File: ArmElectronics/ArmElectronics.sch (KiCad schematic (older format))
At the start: 91 parts, among them J1 Raspberry_Pi_2_3, J10 AH1815 Breakout, J11 AH1815 Breakout, J12 AH1815 Breakout, J13 AH1815 Breakout, J14 AH1815 Breakout, J15 AH1815 Breakout, J16 AH1815 Breakout, J17 AH1815 Breakout, J18 AH1815 Breakout, J19 AH1815 Breakout, J2 Conn_01x14, J20 AH1815 Breakout, J21 1792245, J22 PA-09, J23 PA-09, J24 PA-09, J3 Encoder Breakout, J4 RasPi Power Out, J5 12V In, J6 Batt In, J7 Batt Out, J8 BNO055 QWIIC Conn, J9 AH1815 Breakout, SW1 E-Stop, U1 Teensy4.1, U12 74LVC1G97, U13 74LVC1G97, U14 74LVC1G97, U15 74LVC1G97, U16 74LVC1G97, U17 74LVC1G97, U2 Pololu_2857, U3 MAX11601, U4 Pololu_2851, U5 Pololu_3730, U6 TB9051FTG, U7 TB9051FTG, U8 TB9051FTG

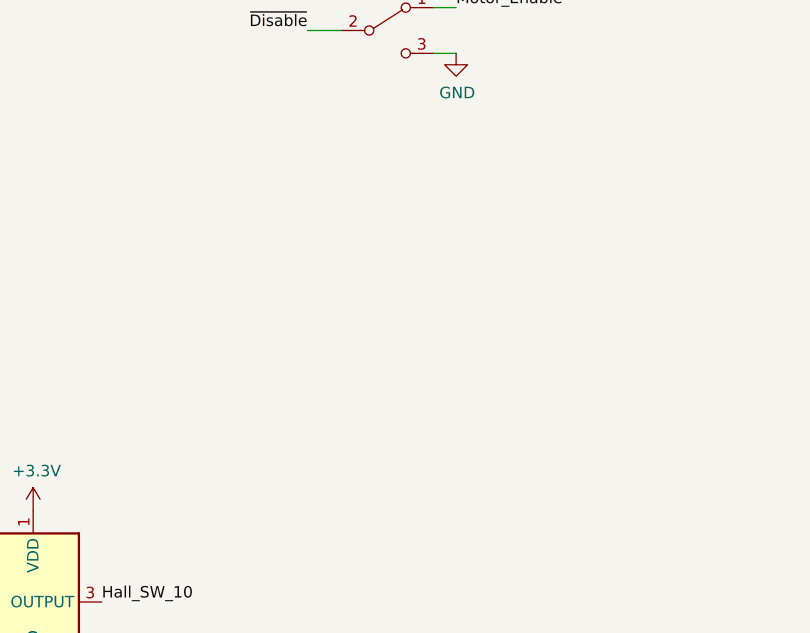
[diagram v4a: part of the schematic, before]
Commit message: Added brake solenoid for axis 0
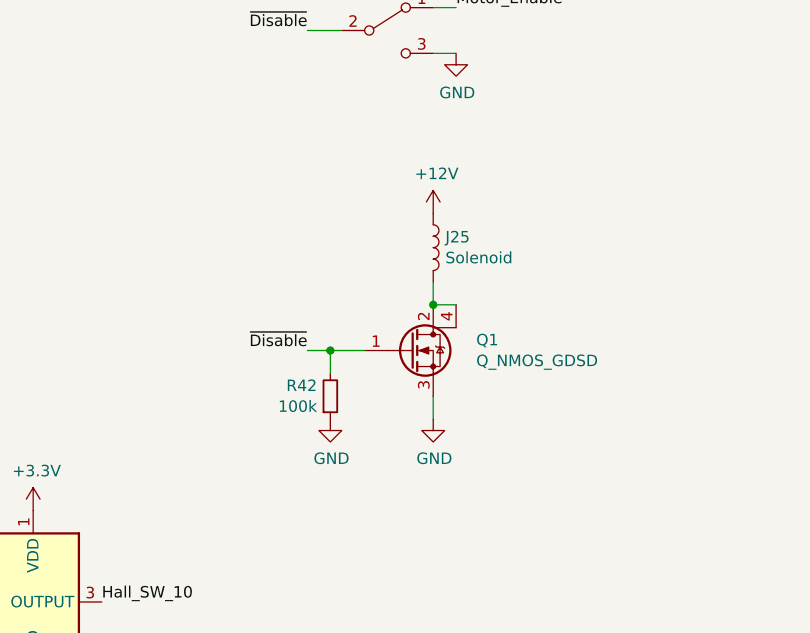
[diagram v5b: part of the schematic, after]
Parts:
- added J25: Solenoid, Connector_JST:JST_XH_B2B-XH-A_1x02_P2.50mm_Vertical, symbol Device:L
- added Q1: Q_NMOS_GDSD, Package_TO_SOT_SMD:SOT-223, symbol Device:Q_NMOS_GDSD
- added R42: 100k, Resistor_SMD:R_0603_1608Metric_Pad1.05x0.95mm_HandSolder, symbol Device:R_Small
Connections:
- net +12V: now also J25.1
- net GND: now also Q1.3 (S), R42.1
- net ~Disable: now also Q1.1 (G), R42.2
- new net: J25.2, Q1.2 (D), Q1.4 (D)
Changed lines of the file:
@@
 Wire Wire Line
 	3100 2250 2900 2250
+$Comp
+L Device:L J25
+U 1 1 5FBC5F32
+P 12950 10450
+F 0 "J25" H 13003 10496 50  0000 L CNN
+F 1 "Solenoid" H 13003 10405 50  0000 L CNN
+F 2 "Connector_JST:JST_XH_B2B-XH-A_1x02_P2.50mm_Vertical" H 12950 10450 50  0001 C CNN
+F 3 "~" H 12950 10450 50  0001 C CNN
+	1    12950 10450
+	1    0    0    -1
+$EndComp
+$Comp
+L Device:Q_NMOS_GDSD Q1
+U 1 1 5FBC8FF5
+P 12850 10900
+F 0 "Q1" H 13138 10946 50  0000 L CNN
+F 1 "Q_NMOS_GDSD" H 13138 10855 50  0000 L CNN
+F 2 "Package_TO_SOT_SMD:SOT-223" H 13050 11000 50  0001 C CNN
+F 3 "~" H 12850 10900 50  0001 C CNN
+F 4 "NCV8440ASTT1GOSCT-ND" H 12850 10900 50  0001 C CNN "Digikey Part Num"
+	1    12850 10900
+	1    0    0    -1
+$EndComp
+$Comp
+L Device:R_Small R42
+U 1 1 5FBCC898
+P 12500 11100
+F 0 "R42" H 12442 11054 50  0000 R CNN
+F 1 "100k" H 12442 11145 50  0000 R CNN
+F 2 "Resistor_SMD:R_0603_1608Metric_Pad1.05x0.95mm_HandSolder" H 12500 11100 50  0001 C CNN
+F 3 "~" H 12500 11100 50  0001 C CNN
+F 4 "P100KGCT-ND" H 12500 11100 50  0001 C CNN "Digikey Part Num"
+	1    12500 11100
+	1    0    0    1
+$EndComp
+Wire Wire Line
+	12400 10900 12500 10900
+Wire Wire Line
+	12500 11000 12500 10900
+Connection ~ 12500 10900
+Wire Wire Line
+	12500 10900 12650 10900
+$Comp
+L power:GND #PWR0126
+U 1 1 5FC1211A
+P 12500 11200
+F 0 "#PWR0126" H 12500 10950 50  0001 C CNN
+F 1 "GND" H 12505 11027 50  0000 C CNN
+F 2 "" H 12500 11200 50  0001 C CNN
+F 3 "" H 12500 11200 50  0001 C CNN
+	1    12500 11200
+	1    0    0    -1
+$EndComp
+Wire Wire Line
+	13050 10700 12950 10700
+Wire Wire Line
+	12950 10700 12950 10600
+Connection ~ 12950 10700
+$Comp
+L power:GND #PWR0127
+U 1 1 5FC36123
+P 12950 11200
+F 0 "#PWR0127" H 12950 10950 50  0001 C CNN
+F 1 "GND" H 12955 11027 50  0000 C CNN
+F 2 "" H 12950 11200 50  0001 C CNN
+F 3 "" H 12950 11200 50  0001 C CNN
+	1    12950 11200
+	1    0    0    -1
+$EndComp
+Wire Wire Line
+	12950 11200 12950 11100
+$Comp
+L power:+12V #PWR060
+U 1 1 5FC71FCB
+P 12950 10300
+F 0 "#PWR060" H 12950 10150 50  0001 C CNN
+F 1 "+12V" H 12965 10473 50  0000 C CNN
+F 2 "" H 12950 10300 50  0001 C CNN
+F 3 "" H 12950 10300 50  0001 C CNN
+	1    12950 10300
+	1    0    0    -1
+$EndComp
+Text Label 12400 10900 2    50   ~ 0
+~Disable
 $EndSCHEMATC

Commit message: Added some 3d models
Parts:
- J10, J11, J12, J13, J14, J15, J16, J17, J18, J19, J20, J9: footprint Connector_JST:JST_PH_S3B-PH-K_1x03_P2.00mm_Horizontal -> Connector_JST:JST_PH_B3B-PH-K_1x03_P2.00mm_Vertical
- J3: footprint Connector_JST:JST_PH_S6B-PH-K_1x06_P2.00mm_Horizontal -> Connector_JST:JST_PH_B6B-PH-K_1x06_P2.00mm_Vertical
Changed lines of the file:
@@
 F 0 "J9" H 7270 12046 50  0000 R CNN
 F 1 "AH1815 Breakout" H 7270 11955 50  0000 R CNN
-F 2 "Connector_JST:JST_PH_S3B-PH-K_1x03_P2.00mm_Horizontal" H 7500 12000 50  0001 C CNN
+F 2 "Connector_JST:JST_PH_B3B-PH-K_1x03_P2.00mm_Vertical" H 7500 12000 50  0001 C CNN
 F 3 "https://www.diodes.com/assets/Datasheets/AH1806.pdf" H 7500 12000 50  0001 C CNN
 	1    7500 12000
@@
 F 0 "J3" H 9480 10592 50  0000 L CNN
 F 1 "Encoder Breakout" H 9480 10501 50  0000 L CNN
-F 2 "Connector_JST:JST_PH_S6B-PH-K_1x06_P2.00mm_Horizontal" H 9400 10600 50  0001 C CNN
+F 2 "Connector_JST:JST_PH_B6B-PH-K_1x06_P2.00mm_Vertical" H 9400 10600 50  0001 C CNN
 F 3 "~" H 9400 10600 50  0001 C CNN
 	1    9400 10600
@@
 F 0 "J10" H 7270 13346 50  0000 R CNN
 F 1 "AH1815 Breakout" H 7270 13255 50  0000 R CNN
-F 2 "Connector_JST:JST_PH_S3B-PH-K_1x03_P2.00mm_Horizontal" H 7500 13300 50  0001 C CNN
+F 2 "Connector_JST:JST_PH_B3B-PH-K_1x03_P2.00mm_Vertical" H 7500 13300 50  0001 C CNN
 F 3 "https://www.diodes.com/assets/Datasheets/AH1806.pdf" H 7500 13300 50  0001 C CNN
 	1    7500 13300
@@
 F 0 "J11" H 7270 14646 50  0000 R CNN
 F 1 "AH1815 Breakout" H 7270 14555 50  0000 R CNN
-F 2 "Connector_JST:JST_PH_S3B-PH-K_1x03_P2.00mm_Horizontal" H 7500 14600 50  0001 C CNN
+F 2 "Connector_JST:JST_PH_B3B-PH-K_1x03_P2.00mm_Vertical" H 7500 14600 50  0001 C CNN
 F 3 "https://www.diodes.com/assets/Datasheets/AH1806.pdf" H 7500 14600 50  0001 C CNN
 	1    7500 14600
@@
 F 0 "J12" H 8520 12046 50  0000 R CNN
 F 1 "AH1815 Breakout" H 8520 11955 50  0000 R CNN
-F 2 "Connector_JST:JST_PH_S3B-PH-K_1x03_P2.00mm_Horizontal" H 8750 12000 50  0001 C CNN
+F 2 "Connector_JST:JST_PH_B3B-PH-K_1x03_P2.00mm_Vertical" H 8750 12000 50  0001 C CNN
 F 3 "https://www.diodes.com/assets/Datasheets/AH1806.pdf" H 8750 12000 50  0001 C CNN
 	1    8750 12000
@@
 F 0 "J13" H 8520 13346 50  0000 R CNN
 F 1 "AH1815 Breakout" H 8520 13255 50  0000 R CNN
-F 2 "Connector_JST:JST_PH_S3B-PH-K_1x03_P2.00mm_Horizontal" H 8750 13300 50  0001 C CNN
+F 2 "Connector_JST:JST_PH_B3B-PH-K_1x03_P2.00mm_Vertical" H 8750 13300 50  0001 C CNN
 F 3 "https://www.diodes.com/assets/Datasheets/AH1806.pdf" H 8750 13300 50  0001 C CNN
 	1    8750 13300
@@
 F 0 "J14" H 8520 14646 50  0000 R CNN
 F 1 "AH1815 Breakout" H 8520 14555 50  0000 R CNN
-F 2 "Connector_JST:JST_PH_S3B-PH-K_1x03_P2.00mm_Horizontal" H 8750 14600 50  0001 C CNN
+F 2 "Connector_JST:JST_PH_B3B-PH-K_1x03_P2.00mm_Vertical" H 8750 14600 50  0001 C CNN
 F 3 "https://www.diodes.com/assets/Datasheets/AH1806.pdf" H 8750 14600 50  0001 C CNN
 	1    8750 14600
@@
 F 0 "J15" H 9720 12046 50  0000 R CNN
 F 1 "AH1815 Breakout" H 9720 11955 50  0000 R CNN
-F 2 "Connector_JST:JST_PH_S3B-PH-K_1x03_P2.00mm_Horizontal" H 9950 12000 50  0001 C CNN
+F 2 "Connector_JST:JST_PH_B3B-PH-K_1x03_P2.00mm_Vertical" H 9950 12000 50  0001 C CNN
 F 3 "https://www.diodes.com/assets/Datasheets/AH1806.pdf" H 9950 12000 50  0001 C CNN
 	1    9950 12000
@@
 F 0 "J16" H 9770 13346 50  0000 R CNN
 F 1 "AH1815 Breakout" H 9770 13255 50  0000 R CNN
-F 2 "Connector_JST:JST_PH_S3B-PH-K_1x03_P2.00mm_Horizontal" H 10000 13300 50  0001 C CNN
+F 2 "Connector_JST:JST_PH_B3B-PH-K_1x03_P2.00mm_Vertical" H 10000 13300 50  0001 C CNN
 F 3 "https://www.diodes.com/assets/Datasheets/AH1806.pdf" H 10000 13300 50  0001 C CNN
 	1    10000 13300
@@
 F 0 "J17" H 9770 14646 50  0000 R CNN
 F 1 "AH1815 Breakout" H 9770 14555 50  0000 R CNN
-F 2 "Connector_JST:JST_PH_S3B-PH-K_1x03_P2.00mm_Horizontal" H 10000 14600 50  0001 C CNN
+F 2 "Connector_JST:JST_PH_B3B-PH-K_1x03_P2.00mm_Vertical" H 10000 14600 50  0001 C CNN
 F 3 "https://www.diodes.com/assets/Datasheets/AH1806.pdf" H 10000 14600 50  0001 C CNN
 	1    10000 14600
@@
 F 0 "J18" H 10970 12046 50  0000 R CNN
 F 1 "AH1815 Breakout" H 10970 11955 50  0000 R CNN
-F 2 "Connector_JST:JST_PH_S3B-PH-K_1x03_P2.00mm_Horizontal" H 11200 12000 50  0001 C CNN
+F 2 "Connector_JST:JST_PH_B3B-PH-K_1x03_P2.00mm_Vertical" H 11200 12000 50  0001 C CNN
 F 3 "https://www.diodes.com/assets/Datasheets/AH1806.pdf" H 11200 12000 50  0001 C CNN
 	1    11200 12000
@@
 F 0 "J19" H 11020 13346 50  0000 R CNN
 F 1 "AH1815 Breakout" H 11020 13255 50  0000 R CNN
-F 2 "Connector_JST:JST_PH_S3B-PH-K_1x03_P2.00mm_Horizontal" H 11250 13300 50  0001 C CNN
+F 2 "Connector_JST:JST_PH_B3B-PH-K_1x03_P2.00mm_Vertical" H 11250 13300 50  0001 C CNN
 F 3 "https://www.diodes.com/assets/Datasheets/AH1806.pdf" H 11250 13300 50  0001 C CNN
 	1    11250 13300
@@
 F 0 "J20" H 11020 14646 50  0000 R CNN
 F 1 "AH1815 Breakout" H 11020 14555 50  0000 R CNN
-F 2 "Connector_JST:JST_PH_S3B-PH-K_1x03_P2.00mm_Horizontal" H 11250 14600 50  0001 C CNN
+F 2 "Connector_JST:JST_PH_B3B-PH-K_1x03_P2.00mm_Vertical" H 11250 14600 50  0001 C CNN
 F 3 "https://www.diodes.com/assets/Datasheets/AH1806.pdf" H 11250 14600 50  0001 C CNN
 	1    11250 14600

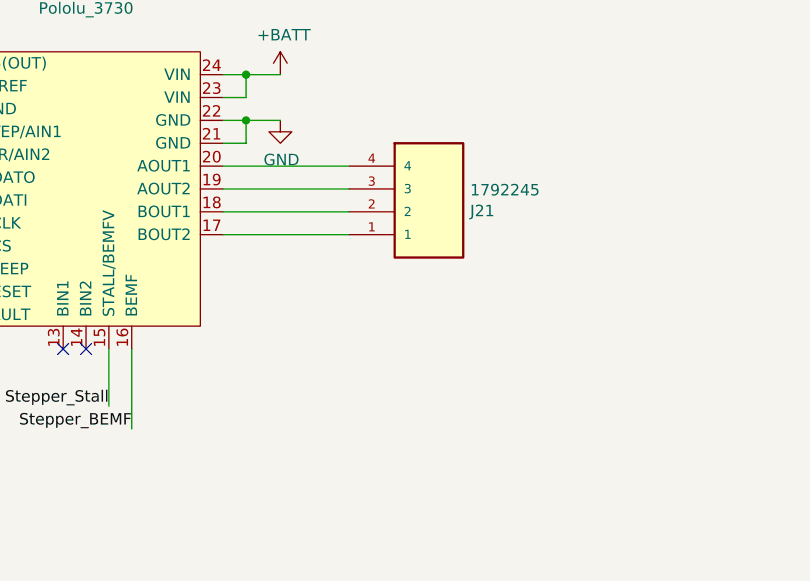
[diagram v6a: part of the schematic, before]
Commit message: added an alternate stepper connector
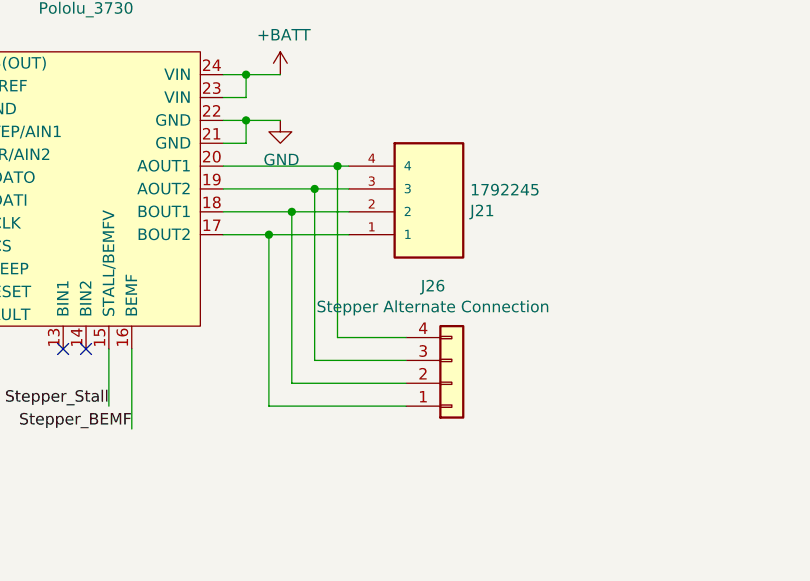
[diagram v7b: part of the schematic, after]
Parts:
- added J26: Stepper Alternate Connection, Connector_JST:JST_XH_S4B-XH-A_1x04_P2.50mm_Horizontal, symbol Connector_Generic:Conn_01x04
- J10, J11, J12, J13, J14, J15, J16, J17, J18, J19, J20, J9, SW1: Digikey Part Num (none) -> 455-1705-ND
- J25: Digikey Part Num (none) -> 455-2247-ND
- J3: Digikey Part Num (none) -> 455-1708-ND
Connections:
- net at J21.1, U5.17 (BOUT2): now also J26.1 (Pin_1)
- net at J21.2, U5.18 (BOUT1): now also J26.2 (Pin_2)
- net at J21.3, U5.19 (AOUT2): now also J26.3 (Pin_3)
- net at J21.4, U5.20 (AOUT1): now also J26.4 (Pin_4)
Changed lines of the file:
@@
 $EndComp
 Wire Wire Line
-	13750 6900 13200 6900
-Wire Wire Line
-	13200 7000 13750 7000
-Wire Wire Line
-	13750 7100 13200 7100
-Wire Wire Line
-	13200 7200 13750 7200
+	13750 6900 13700 6900
+Wire Wire Line
+	13750 7100 13500 7100
+Wire Wire Line
+	13200 7200 13400 7200
 Wire Wire Line
 	13650 3100 13650 2900
@@
 F 2 "Connector_JST:JST_PH_B3B-PH-K_1x03_P2.00mm_Vertical" H 7500 12000 50  0001 C CNN
 F 3 "https://www.diodes.com/assets/Datasheets/AH1806.pdf" H 7500 12000 50  0001 C CNN
+F 4 "455-1705-ND" H 7500 12000 50  0001 C CNN "Digikey Part Num"
 	1    7500 12000
 	1    0    0    -1
@@
 F 2 "Connector_JST:JST_PH_B6B-PH-K_1x06_P2.00mm_Vertical" H 9400 10600 50  0001 C CNN
 F 3 "~" H 9400 10600 50  0001 C CNN
+F 4 "455-1708-ND" H 9400 10600 50  0001 C CNN "Digikey Part Num"
 	1    9400 10600
 	1    0    0    -1
@@
 F 2 "Connector_JST:JST_PH_B3B-PH-K_1x03_P2.00mm_Vertical" H 7500 13300 50  0001 C CNN
 F 3 "https://www.diodes.com/assets/Datasheets/AH1806.pdf" H 7500 13300 50  0001 C CNN
+F 4 "455-1705-ND" H 7500 13300 50  0001 C CNN "Digikey Part Num"
 	1    7500 13300
 	1    0    0    -1
@@
 F 2 "Connector_JST:JST_PH_B3B-PH-K_1x03_P2.00mm_Vertical" H 7500 14600 50  0001 C CNN
 F 3 "https://www.diodes.com/assets/Datasheets/AH1806.pdf" H 7500 14600 50  0001 C CNN
+F 4 "455-1705-ND" H 7500 14600 50  0001 C CNN "Digikey Part Num"
 	1    7500 14600
 	1    0    0    -1
@@
 F 2 "Connector_JST:JST_PH_B3B-PH-K_1x03_P2.00mm_Vertical" H 8750 12000 50  0001 C CNN
 F 3 "https://www.diodes.com/assets/Datasheets/AH1806.pdf" H 8750 12000 50  0001 C CNN
+F 4 "455-1705-ND" H 8750 12000 50  0001 C CNN "Digikey Part Num"
 	1    8750 12000
 	1    0    0    -1
@@
 F 2 "Connector_JST:JST_PH_B3B-PH-K_1x03_P2.00mm_Vertical" H 8750 13300 50  0001 C CNN
 F 3 "https://www.diodes.com/assets/Datasheets/AH1806.pdf" H 8750 13300 50  0001 C CNN
+F 4 "455-1705-ND" H 8750 13300 50  0001 C CNN "Digikey Part Num"
 	1    8750 13300
 	1    0    0    -1
@@
 F 2 "Connector_JST:JST_PH_B3B-PH-K_1x03_P2.00mm_Vertical" H 8750 14600 50  0001 C CNN
 F 3 "https://www.diodes.com/assets/Datasheets/AH1806.pdf" H 8750 14600 50  0001 C CNN
+F 4 "455-1705-ND" H 8750 14600 50  0001 C CNN "Digikey Part Num"
 	1    8750 14600
 	1    0    0    -1
@@
 F 2 "Connector_JST:JST_PH_B3B-PH-K_1x03_P2.00mm_Vertical" H 9950 12000 50  0001 C CNN
 F 3 "https://www.diodes.com/assets/Datasheets/AH1806.pdf" H 9950 12000 50  0001 C CNN
+F 4 "455-1705-ND" H 9950 12000 50  0001 C CNN "Digikey Part Num"
 	1    9950 12000
 	1    0    0    -1
@@
 F 2 "Connector_JST:JST_PH_B3B-PH-K_1x03_P2.00mm_Vertical" H 10000 13300 50  0001 C CNN
 F 3 "https://www.diodes.com/assets/Datasheets/AH1806.pdf" H 10000 13300 50  0001 C CNN
+F 4 "455-1705-ND" H 10000 13300 50  0001 C CNN "Digikey Part Num"
 	1    10000 13300
 	1    0    0    -1
@@
 F 2 "Connector_JST:JST_PH_B3B-PH-K_1x03_P2.00mm_Vertical" H 10000 14600 50  0001 C CNN
 F 3 "https://www.diodes.com/assets/Datasheets/AH1806.pdf" H 10000 14600 50  0001 C CNN
+F 4 "455-1705-ND" H 10000 14600 50  0001 C CNN "Digikey Part Num"
 	1    10000 14600
 	1    0    0    -1
@@
 F 2 "Connector_JST:JST_PH_B3B-PH-K_1x03_P2.00mm_Vertical" H 11200 12000 50  0001 C CNN
 F 3 "https://www.diodes.com/assets/Datasheets/AH1806.pdf" H 11200 12000 50  0001 C CNN
+F 4 "455-1705-ND" H 11200 12000 50  0001 C CNN "Digikey Part Num"
 	1    11200 12000
 	1    0    0    -1
@@
 F 2 "Connector_JST:JST_PH_B3B-PH-K_1x03_P2.00mm_Vertical" H 11250 13300 50  0001 C CNN
 F 3 "https://www.diodes.com/assets/Datasheets/AH1806.pdf" H 11250 13300 50  0001 C CNN
+F 4 "455-1705-ND" H 11250 13300 50  0001 C CNN "Digikey Part Num"
 	1    11250 13300
 	1    0    0    -1
@@
 F 2 "Connector_JST:JST_PH_B3B-PH-K_1x03_P2.00mm_Vertical" H 11250 14600 50  0001 C CNN
 F 3 "https://www.diodes.com/assets/Datasheets/AH1806.pdf" H 11250 14600 50  0001 C CNN
+F 4 "455-1705-ND" H 11250 14600 50  0001 C CNN "Digikey Part Num"
 	1    11250 14600
 	1    0    0    -1
@@
 F 2 "Connector_JST:JST_PH_B3B-PH-K_1x03_P2.00mm_Vertical" H 12750 9500 50  0001 C CNN
 F 3 "~" H 12750 9500 50  0001 C CNN
+F 4 "455-1705-ND" H 12750 9500 50  0001 C CNN "Digikey Part Num"
 	1    12750 9500
 	1    0    0    -1
@@
 F 2 "Connector_JST:JST_XH_B2B-XH-A_1x02_P2.50mm_Vertical" H 12950 10450 50  0001 C CNN
 F 3 "~" H 12950 10450 50  0001 C CNN
+F 4 "455-2247-ND" H 12950 10450 50  0001 C CNN "Digikey Part Num"
 	1    12950 10450
 	1    0    0    -1
@@
 Text Label 12400 10900 2    50   ~ 0
 ~Disable
+$Comp
+L Connector_Generic:Conn_01x04 J26
+U 1 1 5FBD85C2
+P 14200 7850
+F 0 "J26" H 14118 7425 50  0000 C CNN
+F 1 "Stepper Alternate Connection" H 14118 7516 50  0000 C CNN
+F 2 "Connector_JST:JST_XH_S4B-XH-A_1x04_P2.50mm_Horizontal" H 14200 7850 50  0001 C CNN
+F 3 "~" H 14200 7850 50  0001 C CNN
+F 4 "455-2243-ND" H 14200 7850 50  0001 C CNN "Digikey Part Num"
+	1    14200 7850
+	1    0    0    1
+$EndComp
+Wire Wire Line
+	14000 7650 13700 7650
+Wire Wire Line
+	13700 7650 13700 6900
+Connection ~ 13700 6900
+Wire Wire Line
+	13700 6900 13200 6900
+Wire Wire Line
+	14000 7750 13600 7750
+Wire Wire Line
+	13600 7750 13600 7000
+Connection ~ 13600 7000
+Wire Wire Line
+	13600 7000 13750 7000
+Wire Wire Line
+	13200 7000 13600 7000
+Wire Wire Line
+	14000 7850 13500 7850
+Wire Wire Line
+	13500 7850 13500 7100
+Connection ~ 13500 7100
+Wire Wire Line
+	13500 7100 13200 7100
+Wire Wire Line
+	14000 7950 13400 7950
+Wire Wire Line
+	13400 7950 13400 7200
+Connection ~ 13400 7200
+Wire Wire Line
+	13400 7200 13750 7200
 $EndSCHEMATC

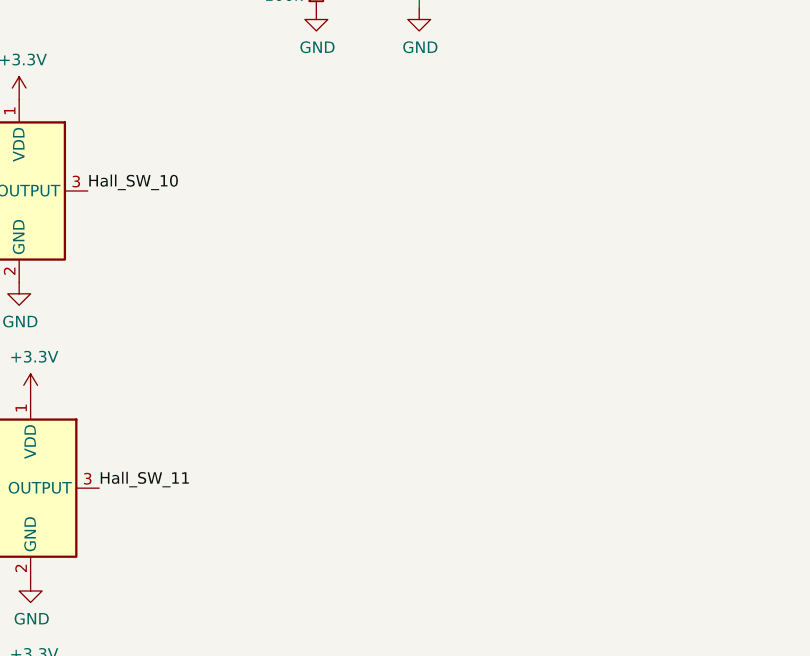
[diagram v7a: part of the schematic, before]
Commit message: Added fan connectors
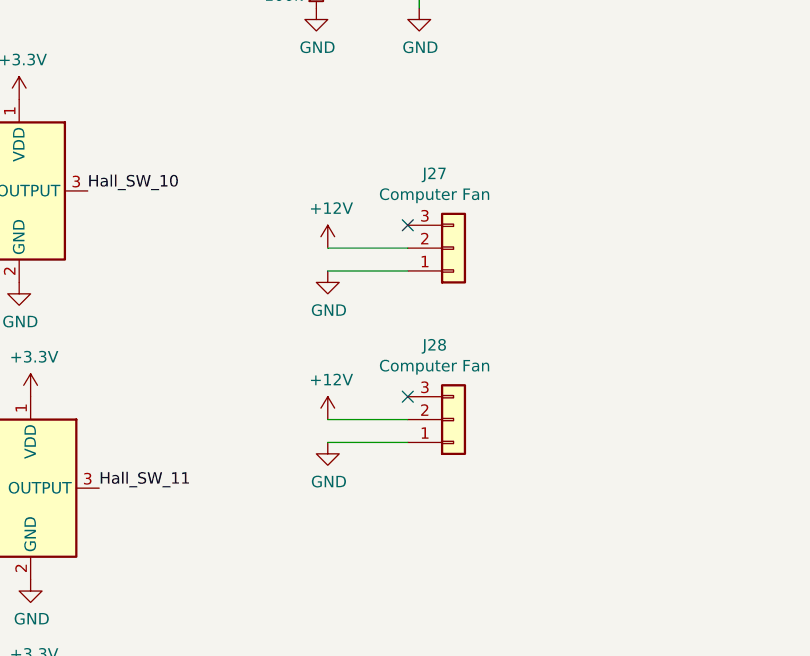
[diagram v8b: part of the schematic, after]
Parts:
- added J27, J28: Computer Fan, Connector_Molex:Molex_KK-254_AE-6410-03A_1x03_P2.54mm_Vertical, symbol Connector_Generic:Conn_01x03
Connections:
- net +12V: now also J27.2 (Pin_2), J28.2 (Pin_2)
- net GND: now also J27.1 (Pin_1), J28.1 (Pin_1)
- no-connect marks 10 -> 12
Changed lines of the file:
@@
 Wire Wire Line
 	13400 7200 13750 7200
+$Comp
+L Connector_Generic:Conn_01x03 J27
+U 1 1 5FC97B21
+P 13100 12250
+F 0 "J27" H 13018 11925 50  0000 C CNN
+F 1 "Computer Fan" H 13018 12016 50  0000 C CNN
+F 2 "Connector_Molex:Molex_KK-254_AE-6410-03A_1x03_P2.54mm_Vertical" H 13100 12250 50  0001 C CNN
+F 3 "~" H 13100 12250 50  0001 C CNN
+F 4 "WM2701-ND" H 13100 12250 50  0001 C CNN "Digikey Part Num"
+	1    13100 12250
+	1    0    0    1
+$EndComp
+$Comp
+L power:GND #PWR062
+U 1 1 5FD09922
+P 12550 12350
+F 0 "#PWR062" H 12550 12100 50  0001 C CNN
+F 1 "GND" H 12555 12177 50  0000 C CNN
+F 2 "" H 12550 12350 50  0001 C CNN
+F 3 "" H 12550 12350 50  0001 C CNN
+	1    12550 12350
+	1    0    0    -1
+$EndComp
+$Comp
+L power:+12V #PWR061
+U 1 1 5FD09ED4
+P 12550 12250
+F 0 "#PWR061" H 12550 12100 50  0001 C CNN
+F 1 "+12V" H 12565 12423 50  0000 C CNN
+F 2 "" H 12550 12250 50  0001 C CNN
+F 3 "" H 12550 12250 50  0001 C CNN
+	1    12550 12250
+	1    0    0    -1
+$EndComp
+Wire Wire Line
+	12550 12250 12900 12250
+Wire Wire Line
+	12900 12350 12550 12350
+NoConn ~ 12900 12150
+$Comp
+L Connector_Generic:Conn_01x03 J28
+U 1 1 5FD7EF5D
+P 13100 13000
+F 0 "J28" H 13018 12675 50  0000 C CNN
+F 1 "Computer Fan" H 13018 12766 50  0000 C CNN
+F 2 "Connector_Molex:Molex_KK-254_AE-6410-03A_1x03_P2.54mm_Vertical" H 13100 13000 50  0001 C CNN
+F 3 "~" H 13100 13000 50  0001 C CNN
+F 4 "WM2701-ND" H 13100 13000 50  0001 C CNN "Digikey Part Num"
+	1    13100 13000
+	1    0    0    1
+$EndComp
+$Comp
+L power:GND #PWR066
+U 1 1 5FD7EF67
+P 12550 13100
+F 0 "#PWR066" H 12550 12850 50  0001 C CNN
+F 1 "GND" H 12555 12927 50  0000 C CNN
+F 2 "" H 12550 13100 50  0001 C CNN
+F 3 "" H 12550 13100 50  0001 C CNN
+	1    12550 13100
+	1    0    0    -1
+$EndComp
+$Comp
+L power:+12V #PWR065
+U 1 1 5FD7EF71
+P 12550 13000
+F 0 "#PWR065" H 12550 12850 50  0001 C CNN
+F 1 "+12V" H 12565 13173 50  0000 C CNN
+F 2 "" H 12550 13000 50  0001 C CNN
+F 3 "" H 12550 13000 50  0001 C CNN
+	1    12550 13000
+	1    0    0    -1
+$EndComp
+Wire Wire Line
+	12550 13000 12900 13000
+Wire Wire Line
+	12900 13100 12550 13100
+NoConn ~ 12900 12900
 $EndSCHEMATC
